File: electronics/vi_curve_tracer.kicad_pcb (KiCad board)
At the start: 2 copper layers, 60 x 37 mm, 65 parts, among them P1 CONN_01X05, P2 USB_OTG, P3 CONN_01X06, P4 CONN_01X06, P5 CONN_01X02, U1 MCP6004, U2 pic24f08km202, U3 ft230x

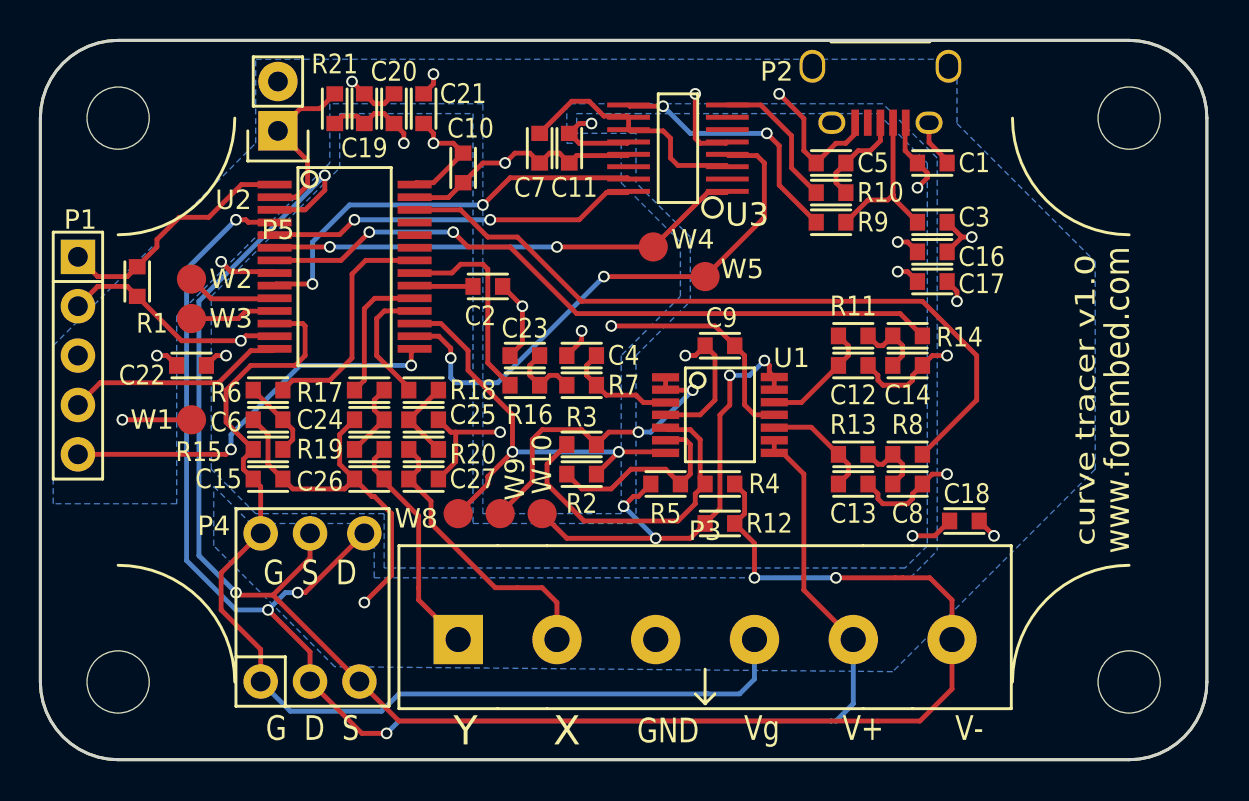
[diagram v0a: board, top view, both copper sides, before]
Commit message: Updated BOM items based on feedback from octopart, added fiducials to layout
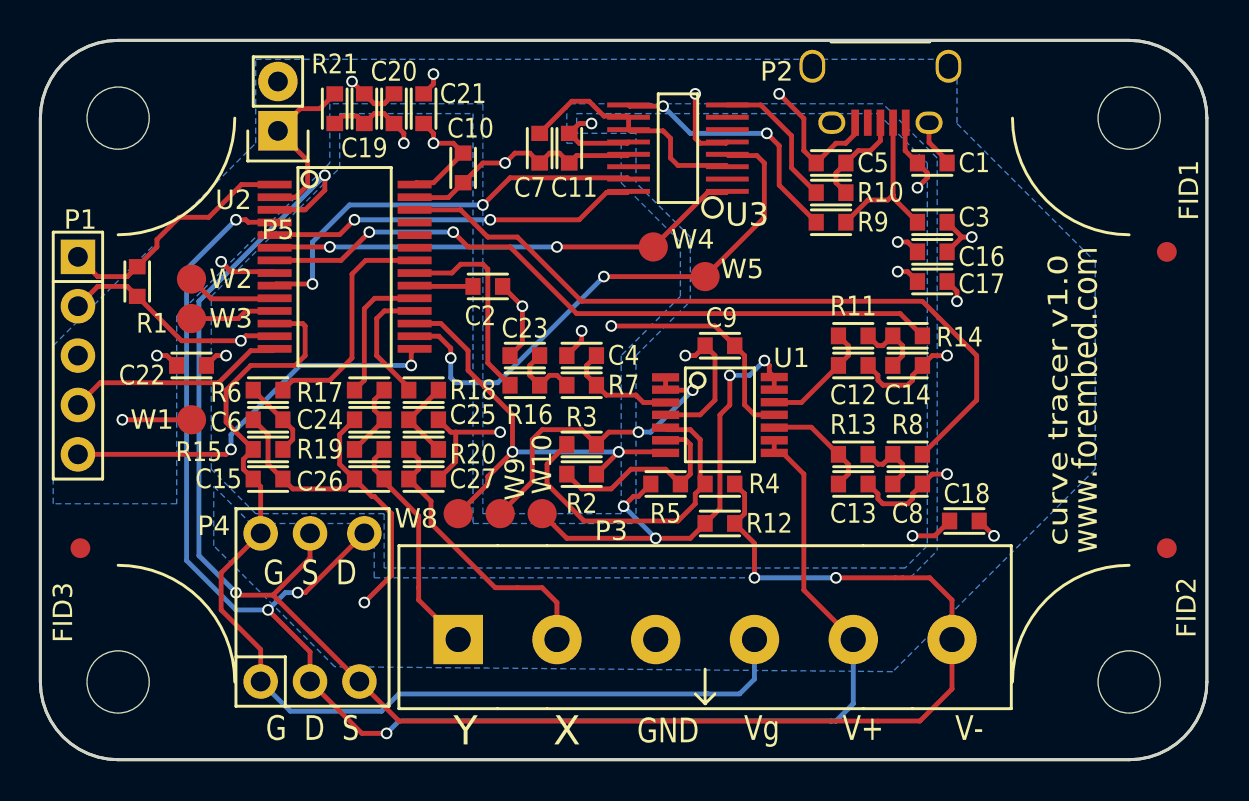
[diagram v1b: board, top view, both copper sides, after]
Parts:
- added FID1: fiducial, fiducial, F.Cu at (224.4, 86.1)
- added FID2: fiducial, kicad_pcb:fiducial, F.Cu at (224.4, 101.3)
- added FID3: fiducial, kicad_pcb:fiducial, F.Cu at (168.5, 101.3)
- renumbered REF** to SOB
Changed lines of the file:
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@@
     (links 136)
     (no_connects 0)
-    (area 166.193999 70.601 226.744001 112.501001)
+    (area 165.444476 70.601 227.493524 112.501001)
     (thickness 1.6)
     (drawings 18)
     (tracks 568)
     (zones 0)
-    (modules 65)
+    (modules 68)
     (nets 44)
   )
@@
     (visible_elements 7FFFFF7F)
     (pcbplotparams
-      (layerselection 0x010f0_80000001)
+      (layerselection 0x210e8_80000001)
       (usegerberextensions false)
       (excludeedgelayer true)
@@
     (add_net ~MCLR)
   )
+  (module fiducial locked (layer F.Cu)
+    (at 224.409 86.106)
+    (fp_text reference FID1 (at 1.143 -3.175 90) (layer F.SilkS)
+      (effects (font (size 1 1) (thickness 0.15)))
+    )
+    (fp_text value fiducial (at 0 0) (layer F.Fab) hide
+      (effects (font (size 1 1) (thickness 0.15)))
+    )
+    (pad 1 smd circle (at 0 0) (size 1.016 1.016) (layers F.Cu F.Mask)
+      (solder_mask_margin 1.016))
+  )
   (module kicad_pcb:case_sickOfBeige_60x37 locked (layer F.Cu)
     (at 196.469 93.726)
-    (fp_text reference REF** (at 0 -22) (layer F.SilkS) hide
+    (fp_text reference SOB (at 0 -22) (layer F.SilkS) hide
       (effects (font (size 1 1) (thickness 0.15)))
     )
@@
   (module kicad_pcb:CONN_1x6_OSTTC062162 (layer F.Cu)
     (at 200.66 106.045)
-    (fp_text reference P3 (at 0 -5.588) (layer F.SilkS)
+    (fp_text reference P3 (at -4.826 -5.588) (layer F.SilkS)
       (effects (font (size 1 1) (thickness 0.15)))
     )
@@
       (net 1 +5V))
   )
+  (module kicad_pcb:fiducial locked (layer F.Cu)
+    (at 224.409 101.346)
+    (fp_text reference FID2 (at 1.016 3.048 90) (layer F.SilkS)
+      (effects (font (size 1 1) (thickness 0.15)))
+    )
+    (fp_text value fiducial (at 0 0) (layer F.Fab) hide
+      (effects (font (size 1 1) (thickness 0.15)))
+    )
+    (pad 1 smd circle (at 0 0) (size 1.016 1.016) (layers F.Cu F.Mask)
+      (solder_mask_margin 1.016))
+  )
+  (module kicad_pcb:fiducial (layer F.Cu)
+    (at 168.529 101.346)
+    (fp_text reference FID3 (at -0.889 3.302 270) (layer F.SilkS)
+      (effects (font (size 1 1) (thickness 0.15)))
+    )
+    (fp_text value fiducial (at 0 0) (layer F.Fab) hide
+      (effects (font (size 1 1) (thickness 0.15)))
+    )
+    (pad 1 smd circle (at 0 0) (size 1.016 1.016) (layers F.Cu F.Mask)
+      (solder_mask_margin 1.016))
+  )
   (gr_text Y (at 188.341 110.744) (layer F.SilkS)
     (effects (font (size 1.5 1.5) (thickness 0.3)))
@@
     (effects (font (size 1.27 1.016) (thickness 0.254)))
   )
-  (gr_text www.forembed.com (at 221.869 93.726 90) (layer F.SilkS)
+  (gr_text www.forembed.com (at 220.218 93.726 90) (layer F.SilkS)
     (effects (font (size 1.27 1.143) (thickness 0.254)))
   )
-  (gr_text "curve tracer v1.0" (at 220.218 93.726 90) (layer F.SilkS)
+  (gr_text "curve tracer v1.0" (at 218.821 93.726 90) (layer F.SilkS)
     (effects (font (size 1.016 1.27) (thickness 0.254)))
   )
@@
   (segment (start 205.74 97.536) (end 205.74 102.87) (width 0.25) (layer F.Cu) (net 18))
   (segment (start 204.6478 96.4438) (end 205.74 97.536) (width 0.25) (layer F.Cu) (net 18) (status 10))
-  (segment (start 205.74 103.505) (end 208.28 106.045) (width 0.25) (layer F.Cu) (net 18) (status 800000))
+  (segment (start 205.74 103.505) (end 208.28 106.045) (width 0.25) (layer F.Cu) (net 18))
   (segment (start 207.137 110.236) (end 207.391 110.236) (width 0.25) (layer B.Cu) (net 18))
   (segment (start 207.391 110.236) (end 208.28 109.347) (width 0.25) (layer B.Cu) (net 18))
-  (segment (start 208.28 109.347) (end 208.28 106.045) (width 0.25) (layer B.Cu) (net 18) (status 800000))
+  (segment (start 208.28 109.347) (end 208.28 106.045) (width 0.25) (layer B.Cu) (net 18))
   (segment (start 207.137 110.236) (end 184.912 110.236) (width 0.25) (layer B.Cu) (net 18))
   (segment (start 180.34 108.204) (end 183.007 110.871) (width 0.25) (layer F.Cu) (net 18))
@@
   (segment (start 184.912 110.236) (end 209.55 110.236) (width 0.25) (layer F.Cu) (net 19))
   (segment (start 182.88 108.204) (end 184.912 110.236) (width 0.25) (layer F.Cu) (net 19) (status 10))
-  (segment (start 213.36 108.585) (end 213.36 106.045) (width 0.25) (layer F.Cu) (net 19) (status 800000))
+  (segment (start 213.36 108.585) (end 213.36 106.045) (width 0.25) (layer F.Cu) (net 19))
   (segment (start 211.709 110.236) (end 213.36 108.585) (width 0.25) (layer F.Cu) (net 19))
   (segment (start 210.82 102.87) (end 212.217 102.87) (width 0.25) (layer F.Cu) (net 19))
   (segment (start 212.217 102.87) (end 213.36 104.013) (width 0.25) (layer F.Cu) (net 19))
-  (segment (start 213.36 104.013) (end 213.36 106.045) (width 0.25) (layer F.Cu) (net 19) (status 800000))
+  (segment (start 213.36 104.013) (end 213.36 106.045) (width 0.25) (layer F.Cu) (net 19))
   (segment (start 203.2 102.87) (end 207.391 102.87) (width 0.25) (layer B.Cu) (net 19))
   (via (at 203.2 102.87) (size 0.6) (drill 0.4) (layers F.Cu B.Cu) (net 19))
@@
   (segment (start 184.912 108.839) (end 200.787 108.839) (width 0.25) (layer B.Cu) (net 36))
   (segment (start 177.8 108.204) (end 179.324 109.728) (width 0.25) (layer B.Cu) (net 36))
-  (segment (start 203.2 108.077) (end 203.2 106.045) (width 0.25) (layer B.Cu) (net 36) (status 800000))
+  (segment (start 203.2 108.077) (end 203.2 106.045) (width 0.25) (layer B.Cu) (net 36))
   (segment (start 202.438 108.839) (end 203.2 108.077) (width 0.25) (layer B.Cu) (net 36))
   (segment (start 177.419 97.79) (end 177.8 98.171) (width 0.25) (layer F.Cu) (net 36) (status 30))
@@
   (segment (start 185.928 99.695) (end 185.928 103.378) (width 0.25) (layer F.Cu) (net 39))
   (segment (start 184.15 97.917) (end 185.928 99.695) (width 0.25) (layer F.Cu) (net 39) (status 10))
-  (segment (start 185.928 104.013) (end 187.96 106.045) (width 0.25) (layer F.Cu) (net 39) (status 800000))
+  (segment (start 185.928 104.013) (end 187.96 106.045) (width 0.25) (layer F.Cu) (net 39))
   (segment (start 184.15 97.79) (end 184.15 97.917) (width 0.25) (layer F.Cu) (net 39) (status 30))
   (segment (start 184.15 96.266) (end 183.642 96.774) (width 0.25) (layer F.Cu) (net 39) (status 10))
@@
   (segment (start 189.865 103.378) (end 191.008 103.378) (width 0.25) (layer F.Cu) (net 40))
   (segment (start 185.42 97.79) (end 186.563 98.933) (width 0.25) (layer F.Cu) (net 40) (status 10))
-  (segment (start 193.04 104.14) (end 193.04 106.045) (width 0.25) (layer F.Cu) (net 40) (status 800000))
+  (segment (start 193.04 104.14) (end 193.04 106.045) (width 0.25) (layer F.Cu) (net 40))
   (segment (start 192.278 103.378) (end 193.04 104.14) (width 0.25) (layer F.Cu) (net 40))
   (segment (start 185.42 96.266) (end 185.928 96.774) (width 0.25) (layer F.Cu) (net 40) (status 10))
